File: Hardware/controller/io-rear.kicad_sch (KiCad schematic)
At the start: 10 parts, among them J601 Conn_02x10_Odd_Even, U601 MCP2542WFD

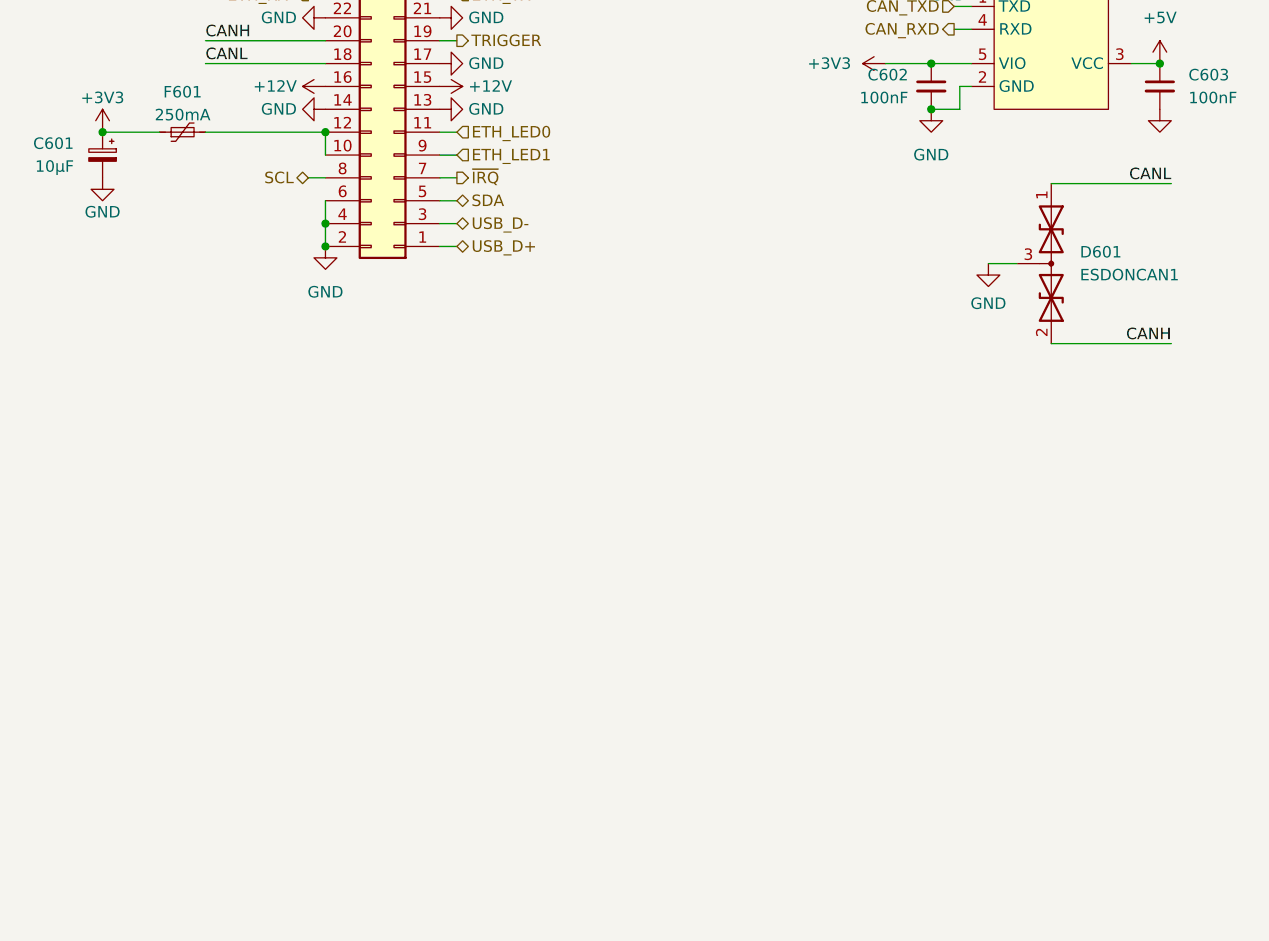
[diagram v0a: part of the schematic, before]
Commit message: More tweaks to controller layout
- Wired up the fan connector to work with PWM control, directly from one
  of the processor's timer/counter's signal generator outputs. For now
  the tachometer output is ignored, but we might do something with it
  later

- Moved around a few passives
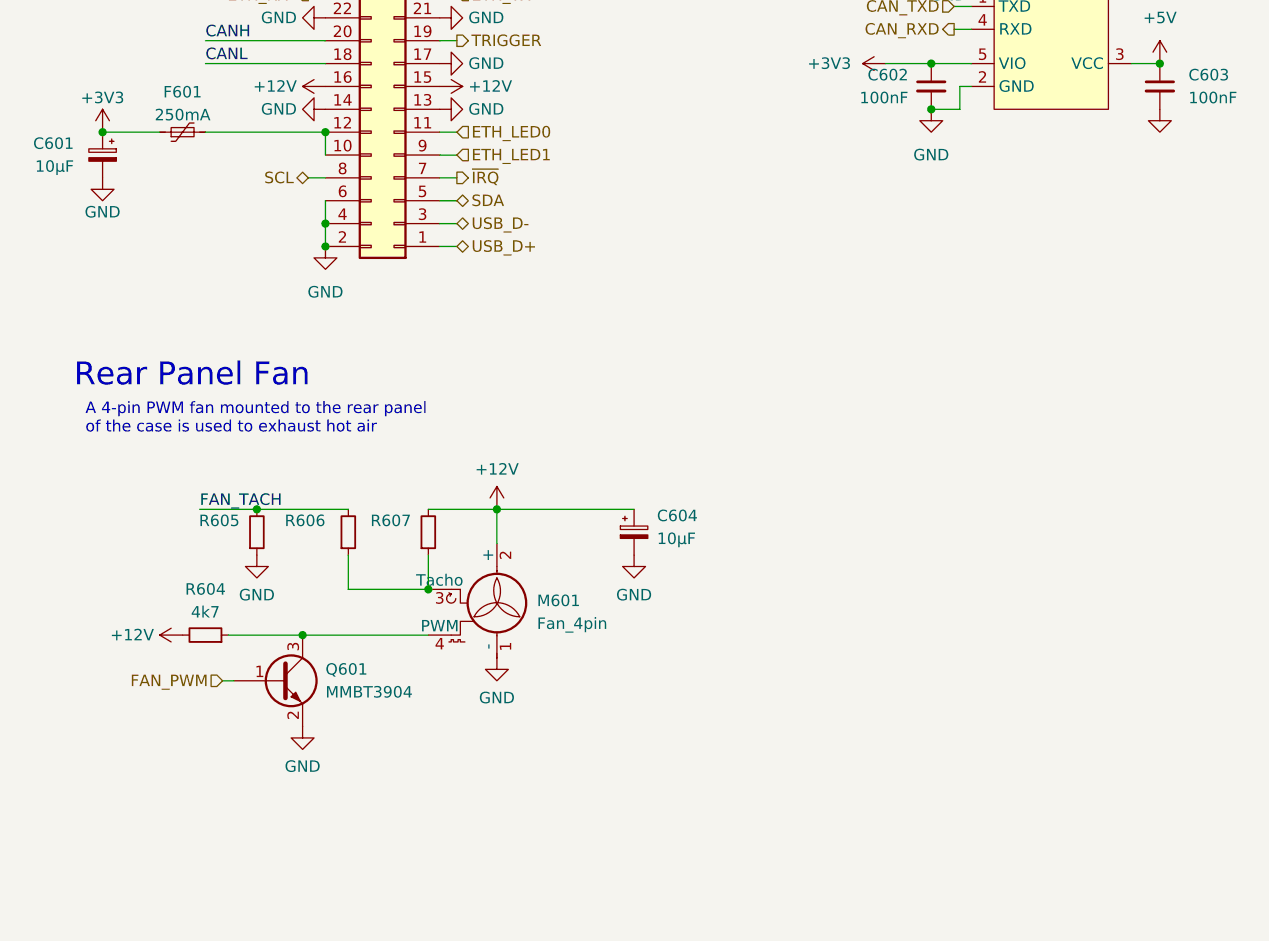
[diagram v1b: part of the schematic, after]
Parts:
- removed D601: ESDONCAN1, Package_TO_SOT_SMD:SOT-23_Handsoldering, symbol Device:D_TVS_Dual_AAC
- added C604: 10µF, Capacitor_THT:CP_Radial_D5.0mm_P2.00mm, symbol Device:C_Polarized_Small
- added M601: Fan_4pin, programmable-load:Molex-47053-1000-MFG, symbol Motor:Fan_4pin
- added Q601: MMBT3904, Package_TO_SOT_SMD:SOT-323_SC-70_Handsoldering, symbol Transistor_BJT:MMBT3904
- added R604: 4k7, Resistor_SMD:R_0805_2012Metric_Pad1.20x1.40mm_HandSolder, symbol Device:R_Small
- added R605, R606, R607: (no value), symbol Device:R_Small
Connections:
- net +12V: now also C604.1, M601.2 (+), R604.2, R607.2
- net GND: now also C604.2, M601.1 (-), Q601.2 (E), R605.1
- new net: M601.3 (Tacho), R606.1, R607.1
- new net: M601.4 (PWM), Q601.3 (C), R604.1
- new net FAN_PWM: Q601.1 (B)
- new net FAN_TACH: R605.2, R606.2
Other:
- note added: "A 4-pin PWM fan mounted to the rear panel of the case is used to exhaust hot air"
- note added: "Rear Panel Fan"

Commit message: Changed analog board connector pinout
- Changed the pinout of the power rails on the analog board to be more
  convenient for the analog board

- Tweaked a few more existing footprints and added some symbols
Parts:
- R605: value (none) -> 10k; footprint (none) -> Resistor_SMD:R_0805_2012Metric_Pad1.20x1.40mm_HandSolder
- R606: value (none) -> 27k4; footprint (none) -> Resistor_SMD:R_0805_2012Metric_Pad1.20x1.40mm_HandSolder
- R607: value (none) -> 4k7; footprint (none) -> Resistor_SMD:R_0805_2012Metric_Pad1.20x1.40mm_HandSolder
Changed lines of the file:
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@@
       (effects (font (size 1.27 1.27)) (justify right))
     )
-    (property "Value" "" (id 1) (at 56.515 99.6949 0)
+    (property "Value" "4k7" (id 1) (at 56.515 99.6949 0)
       (effects (font (size 1.27 1.27)) (justify right))
     )
-    (property "Footprint" "" (id 2) (at 58.42 98.425 0)
+    (property "Footprint" "Resistor_SMD:R_0805_2012Metric_Pad1.20x1.40mm_HandSolder" (id 2) (at 58.42 98.425 0)
       (effects (font (size 1.27 1.27)) hide)
     )
@@
       (effects (font (size 1.27 1.27)) (justify right))
     )
-    (property "Value" "" (id 1) (at 46.99 99.6949 0)
+    (property "Value" "27k4" (id 1) (at 46.99 99.6949 0)
       (effects (font (size 1.27 1.27)) (justify right))
     )
-    (property "Footprint" "" (id 2) (at 49.53 98.425 0)
+    (property "Footprint" "Resistor_SMD:R_0805_2012Metric_Pad1.20x1.40mm_HandSolder" (id 2) (at 49.53 98.425 0)
       (effects (font (size 1.27 1.27)) hide)
     )
@@
       (effects (font (size 1.27 1.27)) (justify right))
     )
-    (property "Value" "" (id 1) (at 37.465 99.6949 0)
+    (property "Value" "10k" (id 1) (at 37.465 99.6949 0)
       (effects (font (size 1.27 1.27)) (justify right))
     )
-    (property "Footprint" "" (id 2) (at 39.37 98.425 0)
+    (property "Footprint" "Resistor_SMD:R_0805_2012Metric_Pad1.20x1.40mm_HandSolder" (id 2) (at 39.37 98.425 0)
       (effects (font (size 1.27 1.27)) hide)
     )

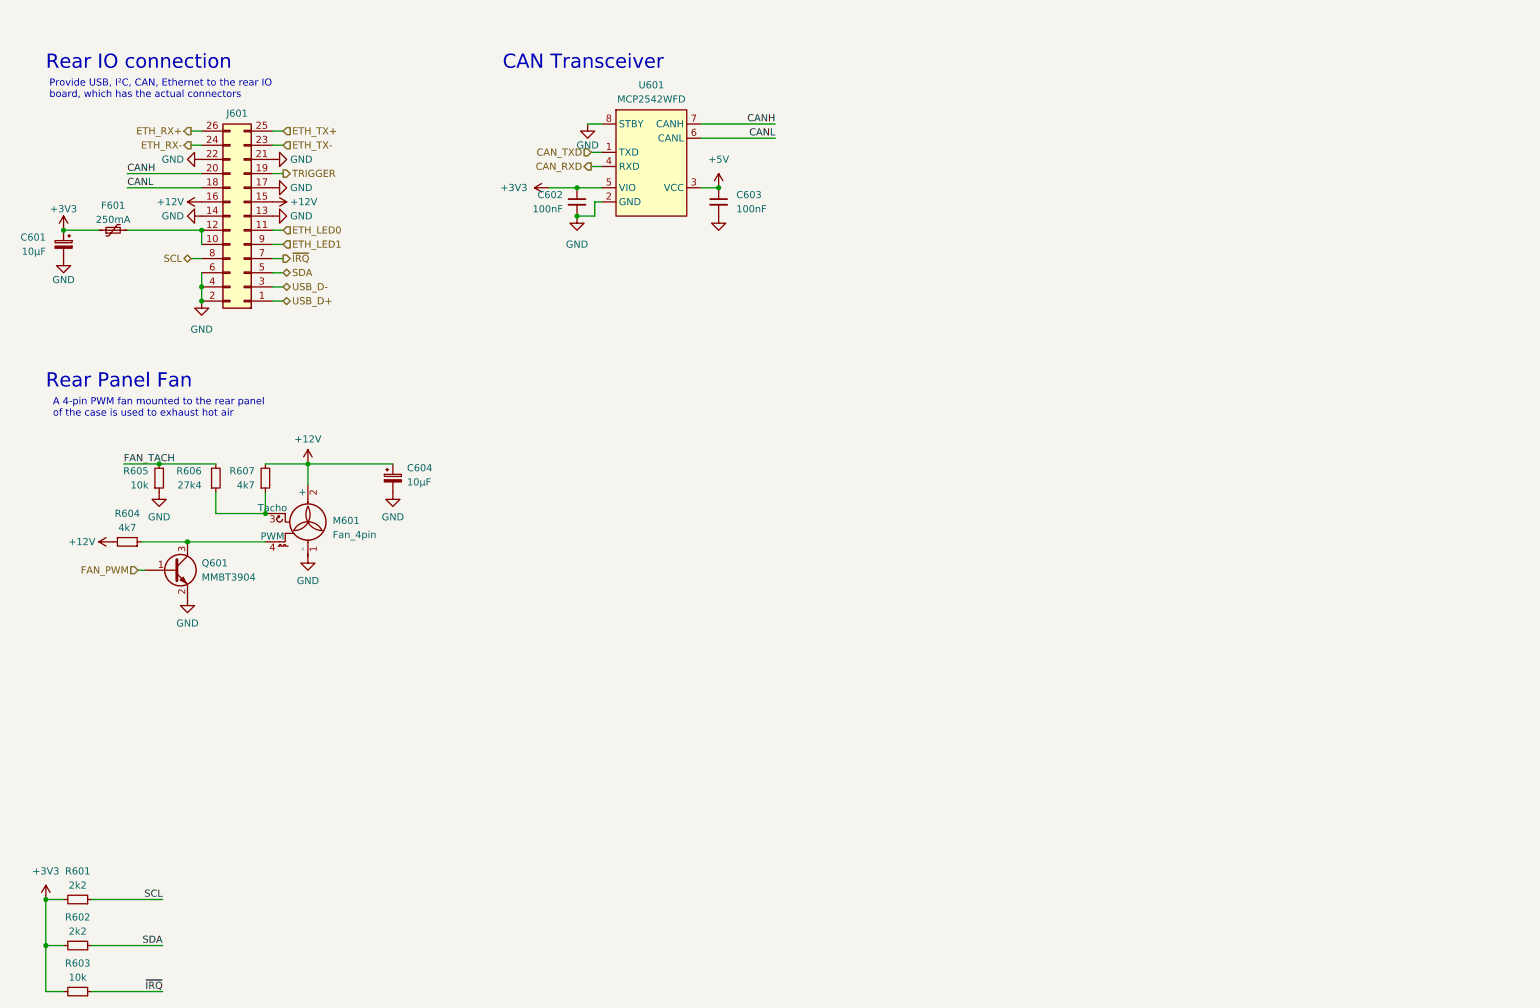
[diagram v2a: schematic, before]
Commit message: Begin cleaning up controller for rework
- Removed some of the old stuff

- Added USB host connector for front panel (including footprint for new
  ESD boi)
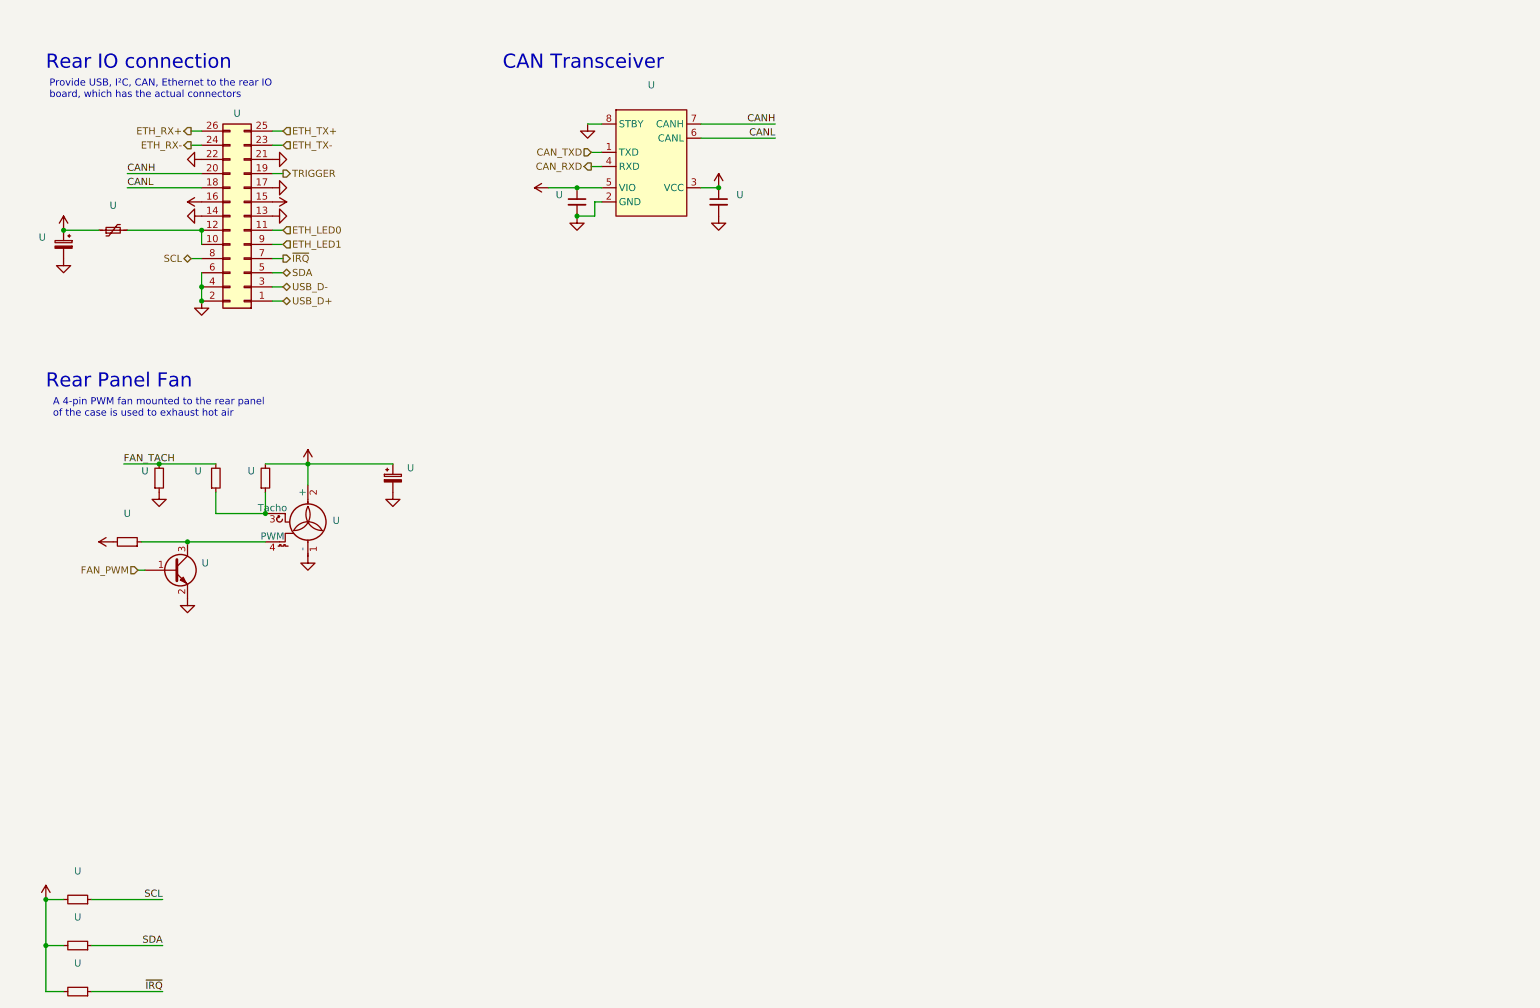
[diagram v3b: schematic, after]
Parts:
- U: renamed from R602; value 2k2 -> (none); footprint Resistor_SMD:R_0805_2012Metric_Pad1.20x1.40mm_HandSolder -> (none)
- U: renamed from U601; value MCP2542WFD -> (none); footprint Package_SO:SOIC-8_3.9x4.9mm_P1.27mm -> (none)
- U: renamed from C603; value 100nF -> (none); footprint Capacitor_SMD:C_0805_2012Metric_Pad1.18x1.45mm_HandSolder -> (none)
- U: renamed from M601; value Fan_4pin -> (none); footprint programmable-load:Molex-47053-1000-MFG -> (none)
- U: renamed from F601; value 250mA -> (none); footprint Fuse:Fuse_1206_3216Metric_Pad1.42x1.75mm_HandSolder -> (none)
- U: renamed from R607; value 4k7 -> (none); footprint Resistor_SMD:R_0805_2012Metric_Pad1.20x1.40mm_HandSolder -> (none)
- U: renamed from R606; value 27k4 -> (none); footprint Resistor_SMD:R_0805_2012Metric_Pad1.20x1.40mm_HandSolder -> (none)
- U: renamed from R603; value 10k -> (none); footprint Resistor_SMD:R_0805_2012Metric_Pad1.20x1.40mm_HandSolder -> (none)
- U: renamed from C601; value 10µF -> (none); footprint Capacitor_Tantalum_SMD:CP_EIA-3216-18_Kemet-A_Pad1.58x1.35mm_HandSolder -> (none)
- U: renamed from R605; value 10k -> (none); footprint Resistor_SMD:R_0805_2012Metric_Pad1.20x1.40mm_HandSolder -> (none)
- U: renamed from C602; value 100nF -> (none); footprint Capacitor_SMD:C_0805_2012Metric_Pad1.18x1.45mm_HandSolder -> (none)
- U: renamed from Q601; value MMBT3904 -> (none); footprint Package_TO_SOT_SMD:SOT-323_SC-70_Handsoldering -> (none)
- U: renamed from R604; value 4k7 -> (none); footprint Resistor_SMD:R_0805_2012Metric_Pad1.20x1.40mm_HandSolder -> (none)
- U: renamed from J601; value Conn_02x10_Odd_Even -> (none); footprint Connector_PinHeader_1.27mm:PinHeader_2x13_P1.27mm_Vertical -> (none)
- U: renamed from R601; value 2k2 -> (none); footprint Resistor_SMD:R_0805_2012Metric_Pad1.20x1.40mm_HandSolder -> (none)
- U: renamed from C604; value 10µF -> (none); footprint Capacitor_THT:CP_Radial_D5.0mm_P2.00mm -> (none)

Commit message: Route controller front panel connections
- Routed the connections to the front panel flex connector (the RGB
  interface, SPI + I2C, and various control signals and its fused power
  rail) and the SoM

- Tweaked SoM symbols and footprint

- Added symbols for 4x 2:1 analog switch (SN74CBTLV3257)
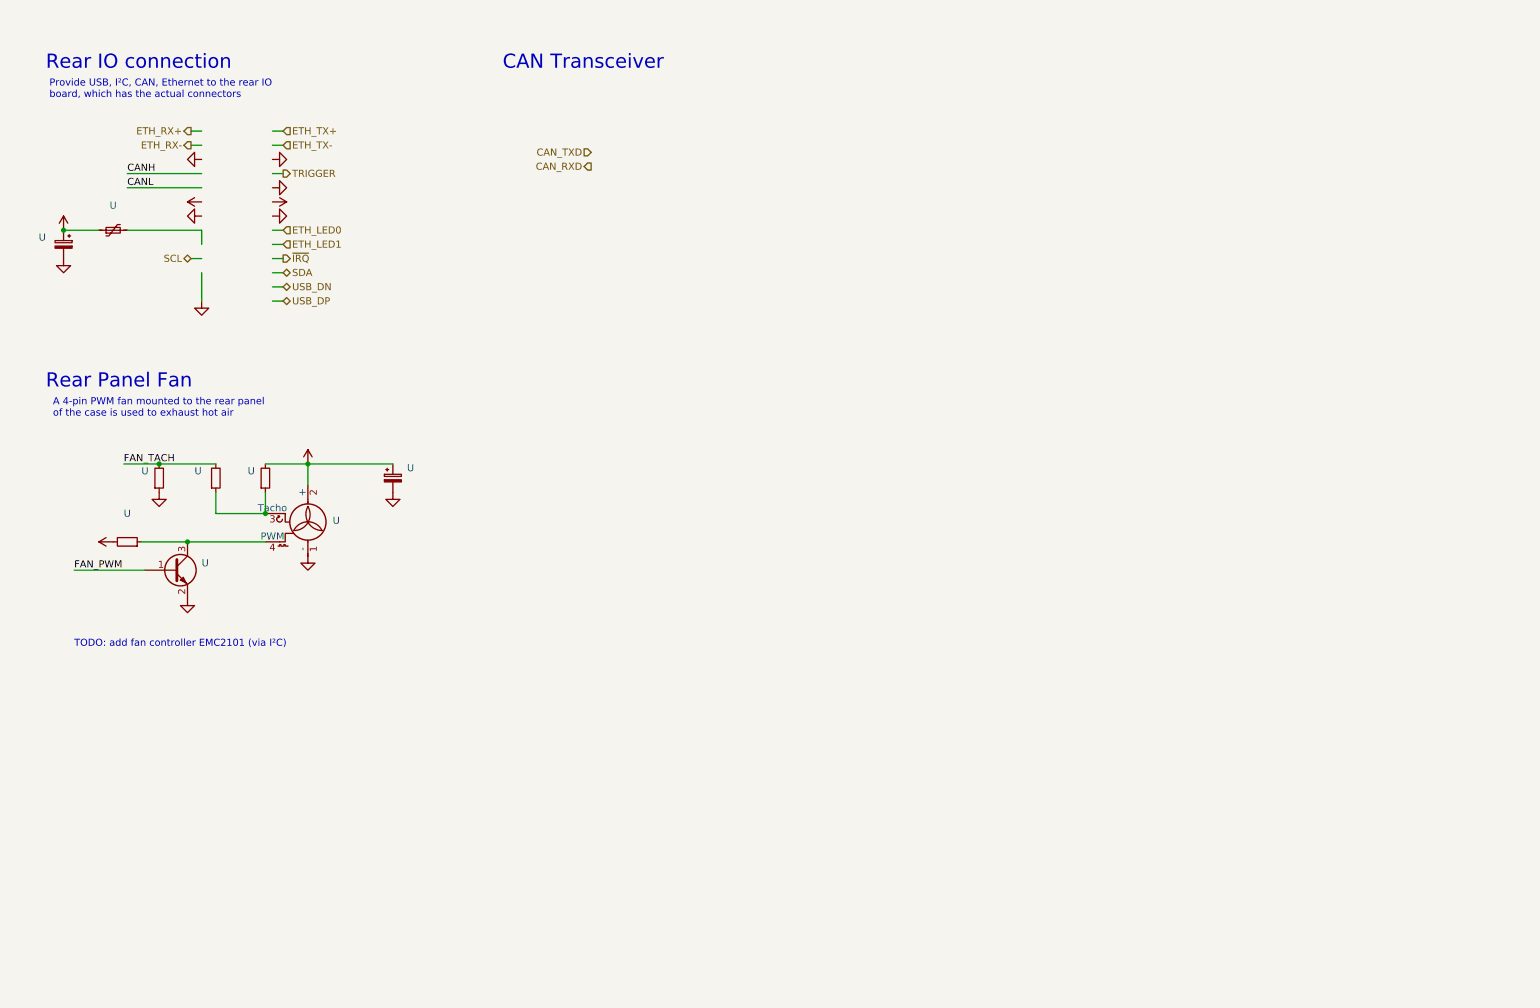
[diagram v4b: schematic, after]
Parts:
- removed U (x3): (no value), symbol Device:R_Small
- removed U: (no value), symbol programmable-load:MCP2542WFD
- removed U (x2): (no value), symbol Device:C_Small
- removed U: (no value), symbol Connector_Generic:Conn_02x13_Odd_Even
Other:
- note added: "TODO: add fan controller EMC2101 (via I²C)"

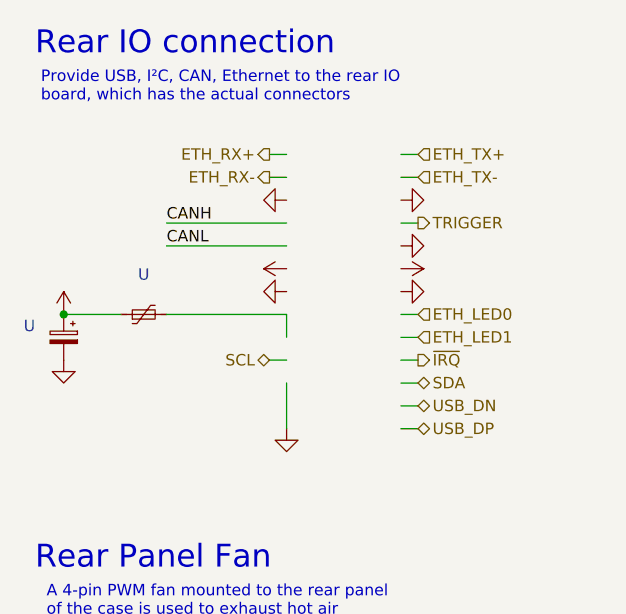
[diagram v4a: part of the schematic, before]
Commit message: More rework of controller
- Updated power section to use a transformer + DC/DC modules, rather
  than a switching AC/DC supply: this should result in fewer bits of
  random noise floating around

- Moved a bunch of stuff around, and changed pinouts slightly of
  external connectors

- Start work on removing dependency on rear IO board

- Minor tweaks to part numbers on front panel board
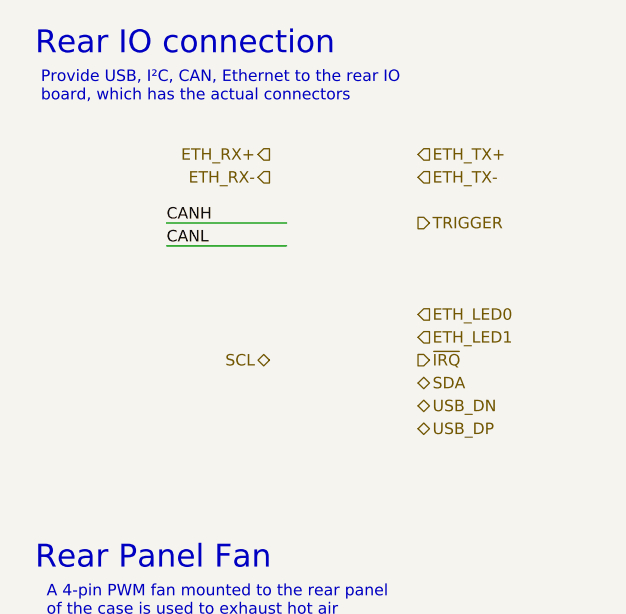
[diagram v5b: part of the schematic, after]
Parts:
- removed U: (no value), symbol Device:Polyfuse_Small
- removed U: (no value), symbol Device:C_Polarized_Small
